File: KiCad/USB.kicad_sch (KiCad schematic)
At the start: 4 parts, among them U9 HT42B534-2

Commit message: Significant schematic changes
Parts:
- added J6: Conn_01x10_Pin, symbol Connector:Conn_01x10_Pin
- added JP7, JP8: Jumper_3_Bridged12, symbol Jumper:Jumper_3_Bridged12
- added R12: R2M, footprint:R0603, symbol Device:R
- added R12: R1M, footprint:R0603, symbol Device:R
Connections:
- net +5V: now also J6.1 (Pin_1), R12.1
- net GND: now also J6.10 (Pin_10), R12.2
- net Rx: now also J6.9 (Pin_9)
- net Tx: now also J6.8 (Pin_8)
- new net Debugger_Potentiometer_signal: JP7.3 (B), JP8.1 (A)
- new net Debugger_SCL: J6.4 (Pin_4)
- new net Debugger_SDA: J6.3 (Pin_3)
- new net Debugger_Thermistor_signal: JP7.1 (A), JP8.3 (B)
- new net Main_Analogue_Data_Read: J6.2 (Pin_2), JP7.2 (C)
- new net Plug_Detect: J6.7 (Pin_7), R12.1, R12.2
- new net Secondary_Analogue_Data_Read: J6.5 (Pin_5), JP8.2 (C)
- no-connect marks 1 -> 2
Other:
- note added: "10 pin debugger"
- title: USB interfacing -> USB interfacing and 10 pin debugger
- moved on the sheet: TP?, U9, U?

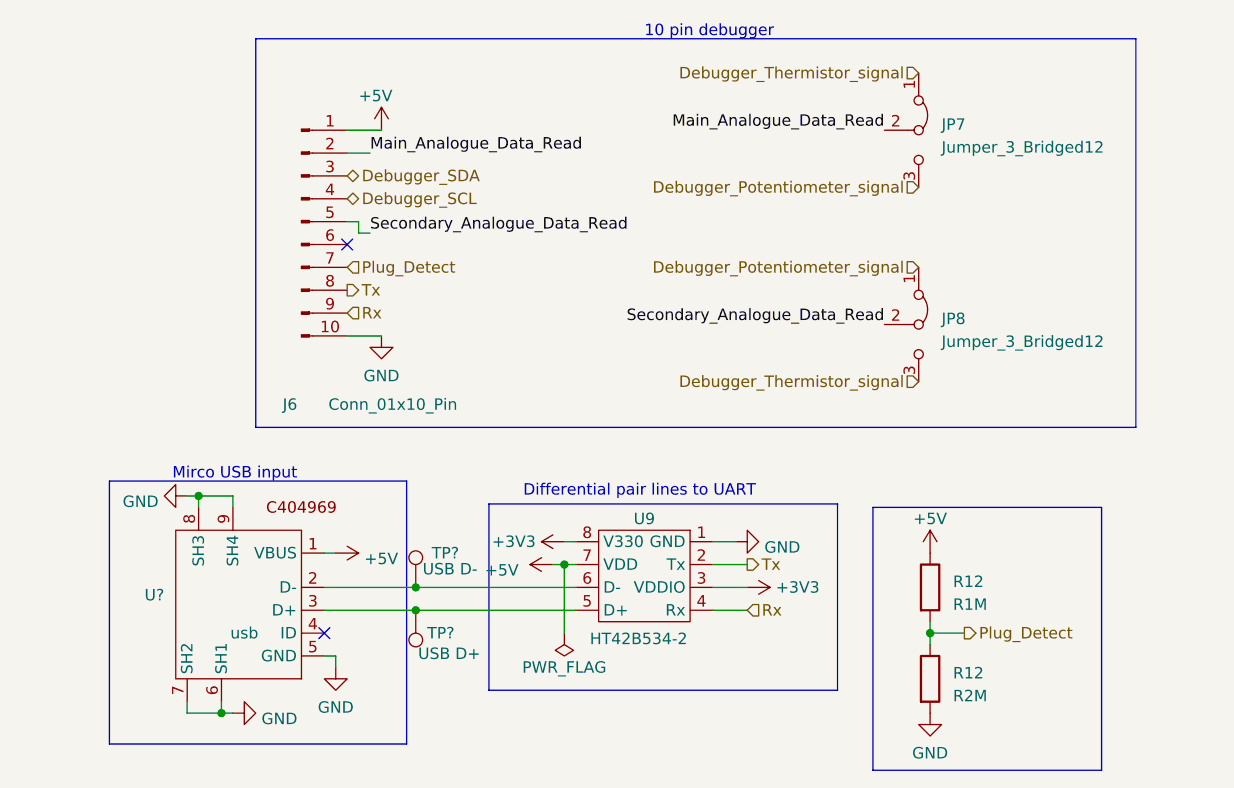
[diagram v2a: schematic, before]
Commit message: Corrected all part numbers and small schematic changes
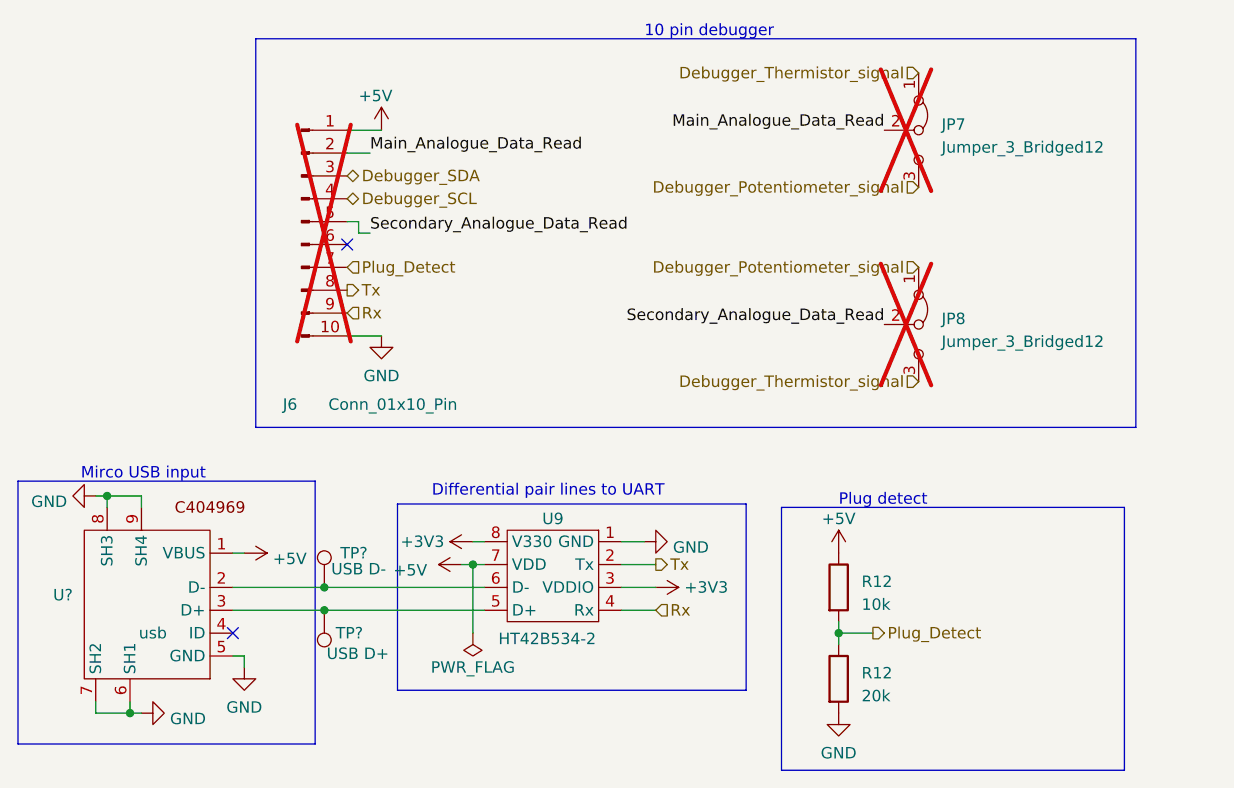
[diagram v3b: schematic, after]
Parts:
- J6, JP7, JP8: Extended Part Cost (none) -> 0; cost per unit (none) -> 0; now not fitted
- R12: value R2M -> 20k; JLC code C23156 -> C4184; Part name 0603WAF3004T5E -> 0603WAF2002T5E; cost per unit 0,0013 -> 0.0010
- R12: value R1M -> 10k; JLC code C23156 -> C17414; Part name 0603WAF3004T5E -> 0805W8F1002T5E; cost per unit 0,0013 -> 0,0010
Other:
- note added: "Plug detect"
- moved on the sheet: R12, TP?, U9, U?

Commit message: Final schematic changes and start board design
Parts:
- added R1: 0, JLCPartFootprints:R0603, symbol Device:R
- J6: value Conn_01x10_Pin -> 01x10_male_header; footprint (none) -> Connector_PinHeader_2.54mm:PinHeader_1x10_P2.54mm_Vertical; DNF (none) -> X
- JP5: renamed from JP7; value Jumper_3_Bridged12 -> 01x03_male_header_jumper; footprint (none) -> Connector_PinHeader_2.54mm:PinHeader_1x03_P2.54mm_Vertical; DNF (none) -> X
- JP6: renamed from JP8; value Jumper_3_Bridged12 -> 01x03_male_header_jumper; footprint (none) -> Connector_PinHeader_2.54mm:PinHeader_1x03_P2.54mm_Vertical; DNF (none) -> X
- R12: footprint footprint:R0603 -> JLCPartFootprints:R0603
- R12: footprint footprint:R0603 -> JLCPartFootprints:R0805
- TP? (x2): footprint footprint:Testpoint_2.54mm -> CustomFootprints:Testpoint; DNF (none) -> X
- U9: footprint footprint:SOIC-8_L4.9-W3.9-P1.27-LS6.0-BL -> JLCPartFootprints:SOP-8_L4.9-W3.9-P1.27-LS6.0-BL
- U?: footprint footprint:MICRO-USB-SMD_MICROXNJ -> JLCPartFootprints:MICRO-USB-SMD_MICROXNJ
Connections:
- net Plug_Detect: now also R1.2; no longer R12.1, R12.2
- new net: R1.1, R12.1, R12.2

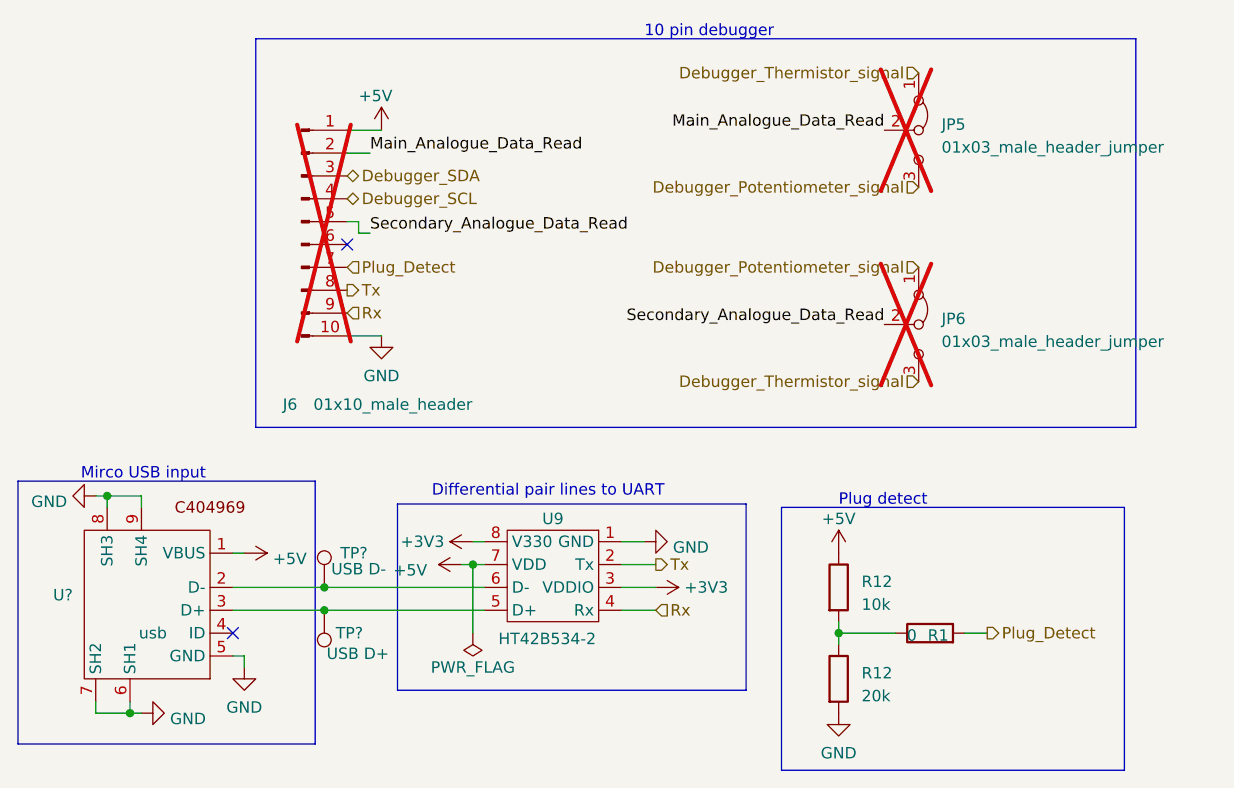
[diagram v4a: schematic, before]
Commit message: literally just added one 0ohm resistor
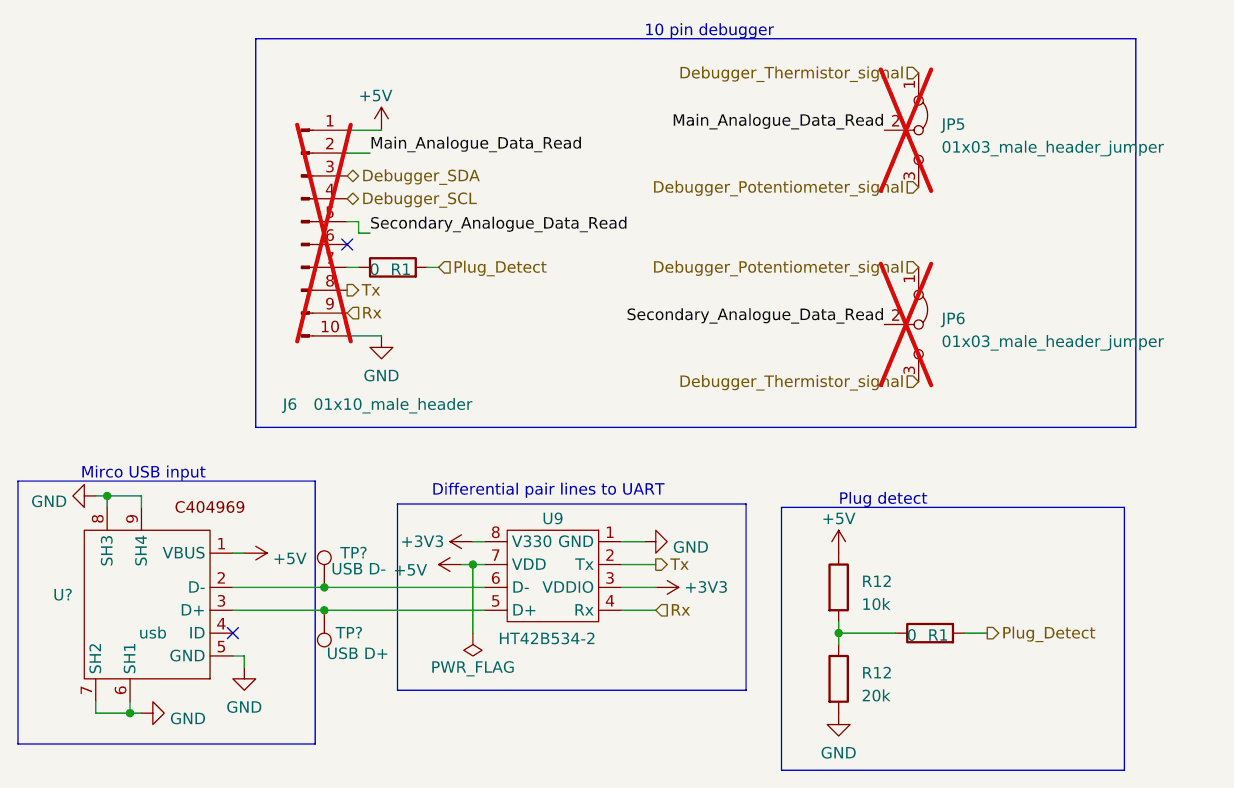
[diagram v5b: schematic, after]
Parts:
- added R1: 0, JLCPartFootprints:R0603, symbol Device:R
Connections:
- net Plug_Detect: now also R1.2; no longer J6.7 (Pin_7)
- new net: J6.7 (Pin_7), R1.1
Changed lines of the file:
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@@
+    (stroke (width 0) (type default))
+  )
+  (wire (pts (xy 191.77 107.95) (xy 193.04 107.95))
     (stroke (width 0) (type default))
   )
@@
   )
   (wire (pts (xy 163.83 133.35) (xy 165.1 133.35))
+    (stroke (width 0) (type default))
+  )
+  (wire (pts (xy 200.66 107.95) (xy 201.93 107.95))
     (stroke (width 0) (type default))
   )
@@
     (effects (font (size 1.27 1.27)) (justify left))
   )
-  (hierarchical_label "Plug_Detect" (shape input) (at 191.77 107.95 0) (fields_autoplaced)
+  (hierarchical_label "Plug_Detect" (shape input) (at 201.93 107.95 0) (fields_autoplaced)
     (effects (font (size 1.27 1.27)) (justify left))
   )
@@
   (symbol (lib_id "power:GND") (at 224.79 138.43 90) (unit 1)
     (in_bom yes) (on_board yes) (dnp no) (fields_autoplaced)
-    (property "Reference" "#PWR054" (at 231.14 138.43 0)
+    (property "Reference" "#PWR053" (at 231.14 138.43 0)
       (effects (font (size 1.27 1.27)) hide)
     )
@@
       (project "EEE3088F_CKR"
         (path "/31e5d740-f3fb-4029-be8d-dfdc4f653d72/4be356fb-1e37-446a-bf93-f98ec62d54dd"
-          (reference "#PWR054") (unit 1)
+          (reference "#PWR053") (unit 1)
         )
       )
@@
         )
         (path "/31e5d740-f3fb-4029-be8d-dfdc4f653d72/4be356fb-1e37-446a-bf93-f98ec62d54dd"
-          (reference "R61") (unit 1)
+          (reference "R60") (unit 1)
         )
       )
@@
   (symbol (lib_id "power:+5V") (at 195.58 92.71 0) (unit 1)
     (in_bom yes) (on_board yes) (dnp no)
-    (property "Reference" "#PWR050" (at 195.58 96.52 0)
+    (property "Reference" "#PWR049" (at 195.58 96.52 0)
       (effects (font (size 1.27 1.27)) hide)
     )
@@
       (project "EEE3088F_CKR"
         (path "/31e5d740-f3fb-4029-be8d-dfdc4f653d72/4be356fb-1e37-446a-bf93-f98ec62d54dd"
-          (reference "#PWR050") (unit 1)
+          (reference "#PWR049") (unit 1)
         )
       )
@@
     )
   )
+  (symbol (lib_id "Device:R") (at 196.85 107.95 90) (unit 1)
+    (in_bom yes) (on_board yes) (dnp no)
+    (property "Reference" "R1" (at 197.739 108.204 90)
+      (effects (font (size 1.27 1.27)))
+    )
+    (property "Value" "0" (at 194.818 108.204 90)
+      (effects (font (size 1.27 1.27)))
+    )
+    (property "Footprint" "JLCPartFootprints:R0603" (at 196.85 109.728 90)
+      (effects (font (size 1.27 1.27)) hide)
+    )
+    (property "Datasheet" "~" (at 196.85 107.95 0)
+      (effects (font (size 1.27 1.27)) hide)
+    )
+    (property "DNF" "" (at 196.85 107.95 0)
+      (effects (font (size 1.27 1.27)) hide)
+    )
+    (property "Extended Part Cost" "0" (at 196.85 107.95 0)
+      (effects (font (size 1.27 1.27)) hide)
+    )
+    (property "JLC code" "C21189" (at 196.85 107.95 0)
+      (effects (font (size 1.27 1.27)) hide)
+    )
+    (property "Part name" "0603WAF0000T5E" (at 196.85 107.95 0)
+      (effects (font (size 1.27 1.27)) hide)
+    )
+    (property "cost per unit" "0,0010" (at 196.85 107.95 0)
+      (effects (font (size 1.27 1.27)) hide)
+    )
+    (pin "1")
+    (pin "2")
+    (instances
+      (project "EEE3088F_CKR"
+        (path "/31e5d740-f3fb-4029-be8d-dfdc4f653d72/781e4e3c-a3ff-4e52-b852-0676e4a3ef49"
+          (reference "R1") (unit 1)
+        )
+        (path "/31e5d740-f3fb-4029-be8d-dfdc4f653d72/4be356fb-1e37-446a-bf93-f98ec62d54dd"
+          (reference "R58") (unit 1)
+        )
+      )
+    )
+  )
   (symbol (lib_id "power:+5V") (at 180.34 139.7 270) (unit 1)
     (in_bom yes) (on_board yes) (dnp no) (fields_autoplaced)
-    (property "Reference" "#PWR048" (at 176.53 139.7 0)
+    (property "Reference" "#PWR047" (at 176.53 139.7 0)
       (effects (font (size 1.27 1.27)) hide)
     )
@@
       (project "EEE3088F_CKR"
         (path "/31e5d740-f3fb-4029-be8d-dfdc4f653d72/4be356fb-1e37-446a-bf93-f98ec62d54dd"
-          (reference "#PWR048") (unit 1)
+          (reference "#PWR047") (unit 1)
         )
       )
@@
   (symbol (lib_id "power:+3V3") (at 226.06 143.51 270) (unit 1)
     (in_bom yes) (on_board yes) (dnp no)
-    (property "Reference" "#PWR055" (at 222.25 143.51 0)
+    (property "Reference" "#PWR054" (at 222.25 143.51 0)
       (effects (font (size 1.27 1.27)) hide)
     )
@@
       (project "EEE3088F_CKR"
         (path "/31e5d740-f3fb-4029-be8d-dfdc4f653d72/4be356fb-1e37-446a-bf93-f98ec62d54dd"
-          (reference "#PWR055") (unit 1)
+          (reference "#PWR054") (unit 1)
         )
       )
@@
   (symbol (lib_id "power:GND") (at 168.91 157.48 90) (unit 1)
     (in_bom yes) (on_board yes) (dnp no) (fields_autoplaced)
-    (property "Reference" "#PWR047" (at 175.26 157.48 0)
+    (property "Reference" "#PWR046" (at 175.26 157.48 0)
       (effects (font (size 1.27 1.27)) hide)
     )
@@
       (project "EEE3088F_CKR"
         (path "/31e5d740-f3fb-4029-be8d-dfdc4f653d72/4be356fb-1e37-446a-bf93-f98ec62d54dd"
-          (reference "#PWR047") (unit 1)
+          (reference "#PWR046") (unit 1)
         )
       )
@@
   (symbol (lib_id "power:GND") (at 195.58 115.57 0) (unit 1)
     (in_bom yes) (on_board yes) (dnp no) (fields_autoplaced)
-    (property "Reference" "#PWR051" (at 195.58 121.92 0)
+    (property "Reference" "#PWR050" (at 195.58 121.92 0)
       (effects (font (size 1.27 1.27)) hide)
     )
@@
       (project "EEE3088F_CKR"
         (path "/31e5d740-f3fb-4029-be8d-dfdc4f653d72/4be356fb-1e37-446a-bf93-f98ec62d54dd"
-          (reference "#PWR051") (unit 1)
+          (reference "#PWR050") (unit 1)
         )
       )
@@
   (symbol (lib_id "power:GND") (at 180.34 152.4 0) (unit 1)
     (in_bom yes) (on_board yes) (dnp no) (fields_autoplaced)
-    (property "Reference" "#PWR049" (at 180.34 158.75 0)
+    (property "Reference" "#PWR048" (at 180.34 158.75 0)
       (effects (font (size 1.27 1.27)) hide)
     )
@@
       (project "EEE3088F_CKR"
         (path "/31e5d740-f3fb-4029-be8d-dfdc4f653d72/4be356fb-1e37-446a-bf93-f98ec62d54dd"
-          (reference "#PWR049") (unit 1)
+          (reference "#PWR048") (unit 1)
         )
       )
@@
         )
         (path "/31e5d740-f3fb-4029-be8d-dfdc4f653d72/4be356fb-1e37-446a-bf93-f98ec62d54dd"
-          (reference "R60") (unit 1)
+          (reference "R59") (unit 1)
         )
       )
@@
   (symbol (lib_id "power:+5V") (at 246.38 139.7 0) (unit 1)
     (in_bom yes) (on_board yes) (dnp no) (fields_autoplaced)
-    (property "Reference" "#PWR056" (at 246.38 143.51 0)
+    (property "Reference" "#PWR055" (at 246.38 143.51 0)
       (effects (font (size 1.27 1.27)) hide)
     )
@@
       (project "EEE3088F_CKR"
         (path "/31e5d740-f3fb-4029-be8d-dfdc4f653d72/4be356fb-1e37-446a-bf93-f98ec62d54dd"
-          (reference "#PWR056") (unit 1)
+          (reference "#PWR055") (unit 1)
         )
       )
@@
   (symbol (lib_id "power:GND") (at 163.83 133.35 270) (unit 1)
     (in_bom yes) (on_board yes) (dnp no) (fields_autoplaced)
-    (property "Reference" "#PWR046" (at 157.48 133.35 0)
+    (property "Reference" "#PWR045" (at 157.48 133.35 0)
       (effects (font (size 1.27 1.27)) hide)
     )
@@
       (project "EEE3088F_CKR"
         (path "/31e5d740-f3fb-4029-be8d-dfdc4f653d72/4be356fb-1e37-446a-bf93-f98ec62d54dd"
-          (reference "#PWR046") (unit 1)
+          (reference "#PWR045") (unit 1)
         )
       )
@@
         )
         (path "/31e5d740-f3fb-4029-be8d-dfdc4f653d72/4be356fb-1e37-446a-bf93-f98ec62d54dd"
-          (reference "R62") (unit 1)
+          (reference "R61") (unit 1)
         )
       )
@@
   (symbol (lib_id "power:+5V") (at 204.47 140.97 90) (unit 1)
     (in_bom yes) (on_board yes) (dnp no) (fields_autoplaced)
-    (property "Reference" "#PWR052" (at 208.28 140.97 0)
+    (property "Reference" "#PWR051" (at 208.28 140.97 0)
       (effects (font (size 1.27 1.27)) hide)
     )
@@
       (project "EEE3088F_CKR"
         (path "/31e5d740-f3fb-4029-be8d-dfdc4f653d72/4be356fb-1e37-446a-bf93-f98ec62d54dd"
-          (reference "#PWR052") (unit 1)
+          (reference "#PWR051") (unit 1)
         )
       )
@@
   (symbol (lib_id "power:GND") (at 246.38 157.48 0) (unit 1)
     (in_bom yes) (on_board yes) (dnp no) (fields_autoplaced)
-    (property "Reference" "#PWR057" (at 246.38 163.83 0)
+    (property "Reference" "#PWR056" (at 246.38 163.83 0)
       (effects (font (size 1.27 1.27)) hide)
     )
@@
       (project "EEE3088F_CKR"
         (path "/31e5d740-f3fb-4029-be8d-dfdc4f653d72/4be356fb-1e37-446a-bf93-f98ec62d54dd"
-          (reference "#PWR057") (unit 1)
+          (reference "#PWR056") (unit 1)
         )
       )
@@
   (symbol (lib_id "power:+3V3") (at 205.74 138.43 90) (unit 1)
     (in_bom yes) (on_board yes) (dnp no)
-    (property "Reference" "#PWR053" (at 209.55 138.43 0)
+    (property "Reference" "#PWR052" (at 209.55 138.43 0)
       (effects (font (size 1.27 1.27)) hide)
     )
@@
       (project "EEE3088F_CKR"
         (path "/31e5d740-f3fb-4029-be8d-dfdc4f653d72/4be356fb-1e37-446a-bf93-f98ec62d54dd"
-          (reference "#PWR053") (unit 1)
-        )
-      )
+          (reference "#PWR052") (unit 1)
+        )
+      )
